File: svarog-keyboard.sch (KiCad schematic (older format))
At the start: 314 parts, among them J1 AVR-ISP-6, J10 I2C, J2 Conn_01x08_Male, J3 I2C, J4 I2C, J5 I2C, J6 I2C, J7 I2C, J8 I2C, J9 I2C, K1 KEYSW, K10 KEYSW, K11 KEYSW, K12 KEYSW, K13 KEYSW, K13-1 KEYSW, K14 KEYSW, K14-1 KEYSW, K14-2 KEYSW, K15 KEYSW, K16 KEYSW, K17 KEYSW, K18 KEYSW, K19 KEYSW, K2 KEYSW, K20 KEYSW, K21 KEYSW, K3 KEYSW, K4 KEYSW, K5 KEYSW, K6 KEYSW, K7 KEYSW, K8 KEYSW, K9 KEYSW, SW1 SW_BOOT, SW2 SW_RESET, U1 ATmega32A-PU, U2 MCP23017_SP, U3 MCP23017_SP, U4 MCP23017_SP, Y1 Crystal

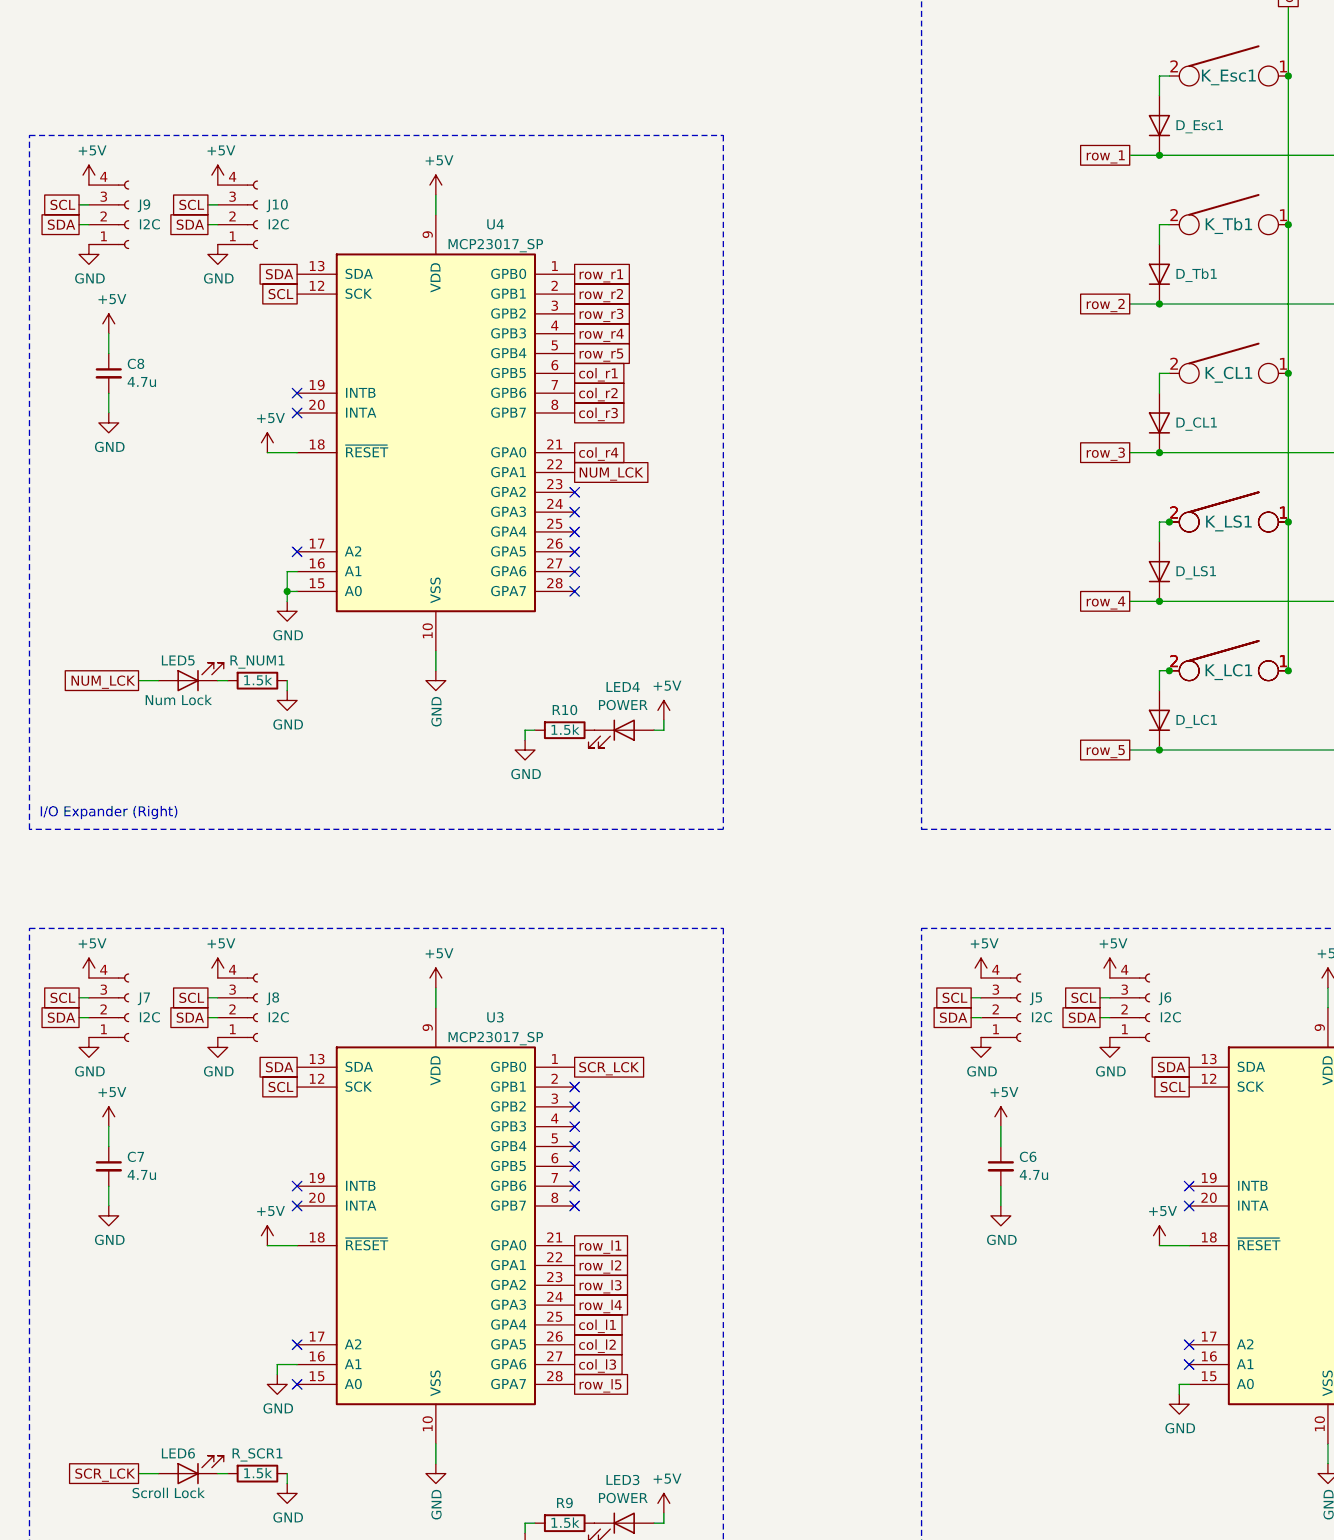
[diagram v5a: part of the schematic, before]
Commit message: Removed Traces, cleanup
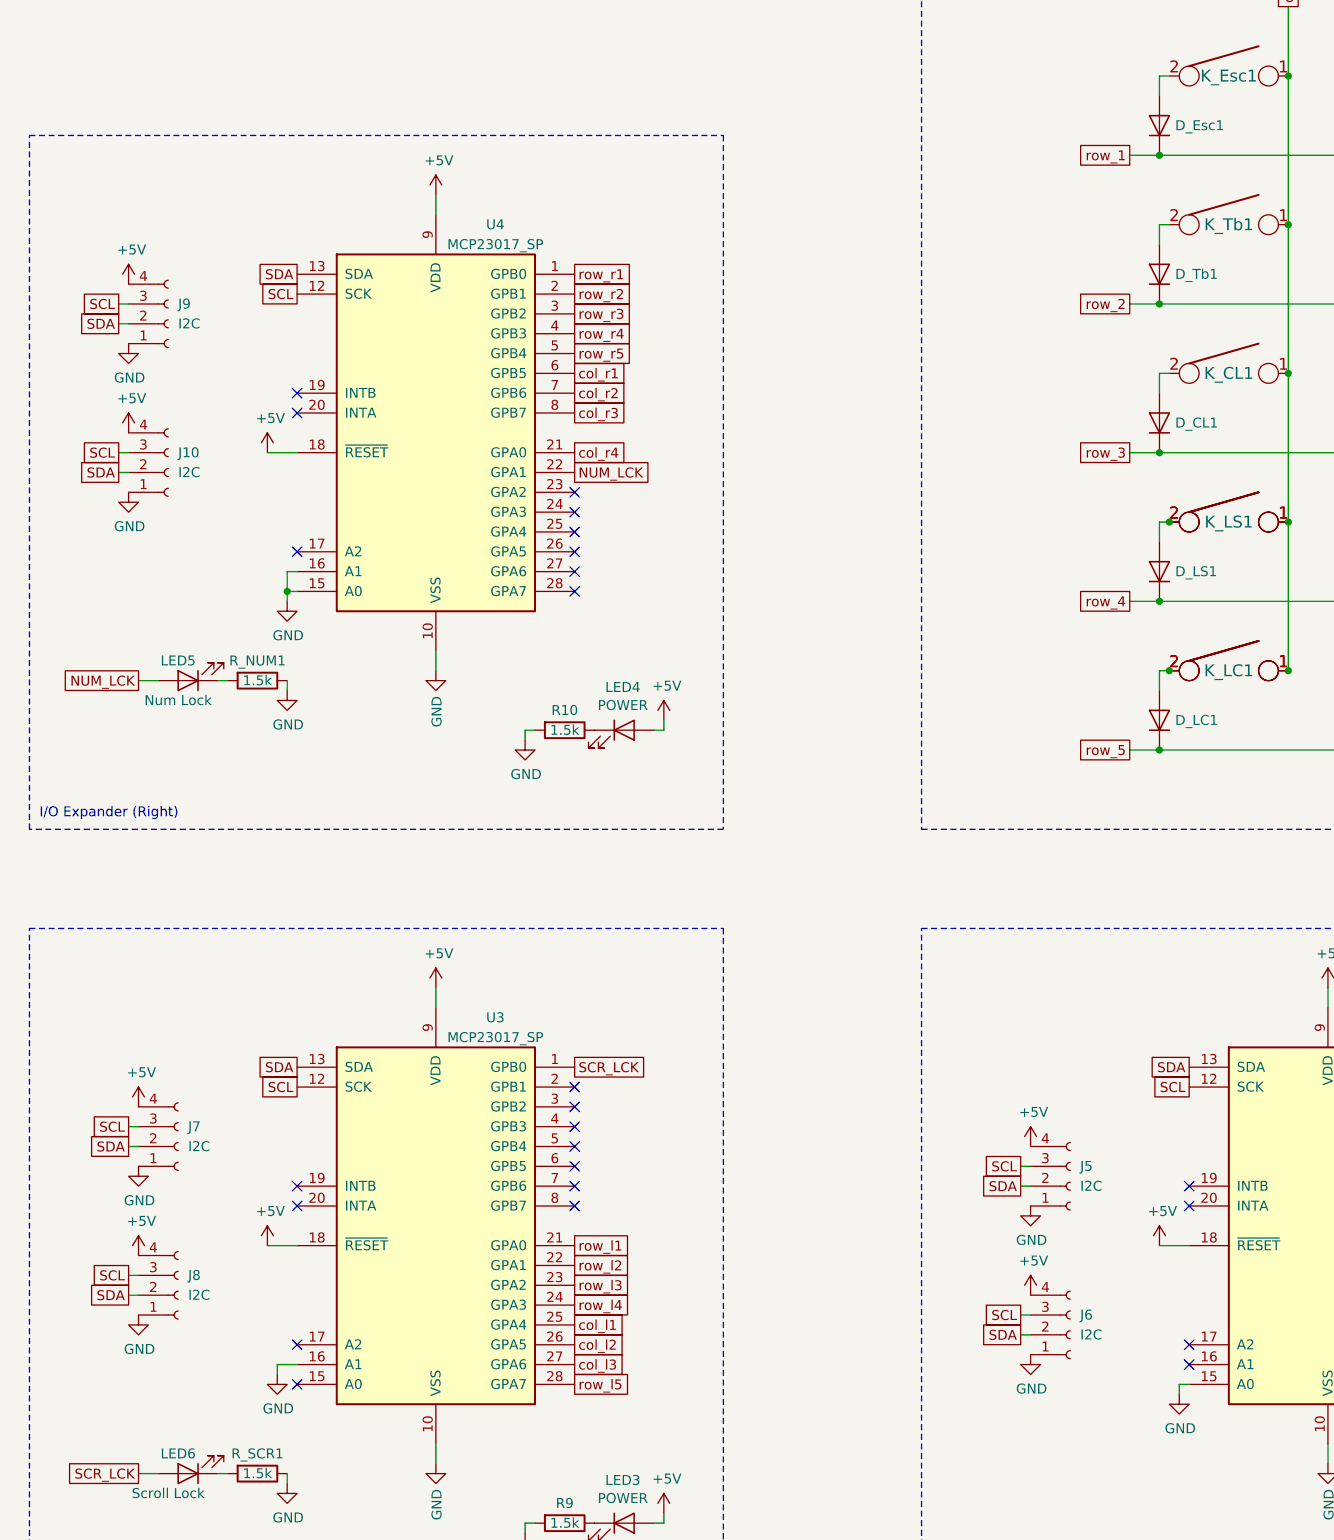
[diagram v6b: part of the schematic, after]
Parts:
- removed C6, C7, C8: 4.7u, Capacitor_THT:CP_Radial_D4.0mm_P1.50mm, symbol Device:C_Small
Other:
- moved on the sheet: J10, J5, J6, J7, J8, J9

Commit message: Wired [TODO] main matrix and [FULL] side matrixes
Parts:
- K_RS1-1.75u1: renamed from K_RS1-1.25u1; footprint Button_Switch_Keyboard:SW_Cherry_MX_1.25u_PCB -> Button_Switch_Keyboard:SW_Cherry_MX_1.75u_PCB
- K_RS1-1u1: renamed from K_RS1-1.5u1; footprint Button_Switch_Keyboard:SW_Cherry_MX_1.50u_PCB -> Button_Switch_Keyboard:SW_Cherry_MX_1.00u_PCB
- K_RS2: footprint Button_Switch_Keyboard:SW_Cherry_MX_1.50u_PCB -> Button_Switch_Keyboard:SW_Cherry_MX_1.00u_PCB
- K_RS2-1.75u1: renamed from K_RS2-1.25u1; footprint Button_Switch_Keyboard:SW_Cherry_MX_1.25u_PCB -> Button_Switch_Keyboard:SW_Cherry_MX_1.75u_PCB
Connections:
- net NUM_LCK: now also U4.1 (GPB0); no longer U4.22 (GPA1)
- net col_1: now also U1.1 (PB0); no longer U1.38 (PA2)
- net col_3: now also U1.2 (PB1); no longer U1.37 (PA3)
- net col_5: now also U1.3 (PB2); no longer U1.36 (PA4)
- net col_r1: now also U4.8 (GPB7); no longer U4.6 (GPB5)
- net col_r3: now also U4.6 (GPB5); no longer U4.8 (GPB7)
- net col_r4: now also U4.5 (GPB4); no longer U4.21 (GPA0)
- net row_1: now also U1.36 (PA4); no longer U1.3 (PB2)
- net row_2: now also U1.37 (PA3); no longer U1.39 (PA1)
- net row_3: now also U1.38 (PA2); no longer U1.2 (PB1)
- net row_4: now also D_RS2.1 (K), U1.39 (PA1); no longer U1.40 (PA0)
- net row_5: now also U1.40 (PA0); no longer U1.1 (PB0)
- net row_r1: now also U4.21 (GPA0); no longer U4.1 (GPB0)
- net row_r2: now also U4.25 (GPA4); no longer U4.2 (GPB1)
- net row_r3: now also U4.26 (GPA5); no longer U4.3 (GPB2)
- net row_r4: now also U4.27 (GPA6); no longer U4.4 (GPB3)
- net row_r5: now also U4.28 (GPA7); no longer U4.5 (GPB4)
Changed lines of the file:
@@
 Wire Wire Line
 	7500 2450 7750 2450
+Text GLabel 3350 1550 2    50   UnSpc ~ 0
+row_4
+Text GLabel 3350 1750 2    50   UnSpc ~ 0
+row_2
+Text GLabel 3350 2350 2    50   UnSpc ~ 0
+col_1
+Text GLabel 3350 2450 2    50   UnSpc ~ 0
+col_3
+Text GLabel 3350 2550 2    50   UnSpc ~ 0
+col_5
 Text GLabel 3350 1450 2    50   UnSpc ~ 0
-row_4
-Text GLabel 3350 1550 2    50   UnSpc ~ 0
-row_2
+row_5
 Text GLabel 3350 1650 2    50   UnSpc ~ 0
-col_1
-Text GLabel 3350 1750 2    50   UnSpc ~ 0
-col_3
+row_3
 Text GLabel 3350 1850 2    50   UnSpc ~ 0
-col_5
-Text GLabel 3350 2350 2    50   UnSpc ~ 0
-row_5
-Text GLabel 3350 2450 2    50   UnSpc ~ 0
-row_3
-Text GLabel 3350 2550 2    50   UnSpc ~ 0
 row_1
 Text GLabel 3350 2650 2    50   UnSpc ~ 0
@@
 NoConn ~ 2350 8900
 NoConn ~ 2350 9600
-NoConn ~ 3750 9700
-NoConn ~ 3750 9800
 Wire Notes Line
 	4500 7500 4500 11000
@@
 Text GLabel 3750 13700 2    50   UnSpc ~ 0
 col_l3
-NoConn ~ 3750 9600
 NoConn ~ 3750 9400
 NoConn ~ 3750 9300
-NoConn ~ 3750 9500
-Text GLabel 3750 8200 2    50   UnSpc ~ 0
-row_r1
-Text GLabel 3750 8300 2    50   UnSpc ~ 0
-row_r2
-Text GLabel 3750 8400 2    50   UnSpc ~ 0
-row_r3
-Text GLabel 3750 8500 2    50   UnSpc ~ 0
-row_r4
-Text GLabel 3750 8600 2    50   UnSpc ~ 0
-row_r5
-Text GLabel 3750 8700 2    50   UnSpc ~ 0
+Text GLabel 3750 8900 2    50   UnSpc ~ 0
 col_r1
 Text GLabel 3750 8800 2    50   UnSpc ~ 0
 col_r2
-Text GLabel 3750 8900 2    50   UnSpc ~ 0
+Text GLabel 3750 8700 2    50   UnSpc ~ 0
 col_r3
-Text GLabel 3750 9100 2    50   UnSpc ~ 0
-col_r4
 $Comp
 L power:GND #PWR0134
@@
 Text GLabel 3350 1950 2    50   UnSpc ~ 0
 CPS_LCK
-Text GLabel 3750 9200 2    50   UnSpc ~ 0
+Text GLabel 3750 8200 2    50   UnSpc ~ 0
 NUM_LCK
 Text GLabel 3750 12200 2    50   UnSpc ~ 0
@@
 Connection ~ 19700 9850
 Wire Wire Line
-	19700 9850 21500 9850
+	19700 9850 20700 9850
 Wire Wire Line
 	20350 8700 20350 9450
@@
 F 0 "K_RS2" H 21050 9450 60  0000 C CNN
 F 1 "KEYSW" H 21050 9350 60  0001 C CNN
-F 2 "Button_Switch_Keyboard:SW_Cherry_MX_1.50u_PCB" H 21050 9450 60  0001 C CNN
+F 2 "Button_Switch_Keyboard:SW_Cherry_MX_1.00u_PCB" H 21050 9450 60  0001 C CNN
 F 3 "" H 21050 9450 60  0000 C CNN
 	1    21050 9450
@@
 	20700 9450 20700 9550
 $Comp
-L keyboard_parts:KEYSW K_RS1-1.5u1
+L keyboard_parts:KEYSW K_RS1-1u1
 U 1 1 5ED8F2CF
 P 20050 9450
-F 0 "K_RS1-1.5u1" H 20050 9450 60  0001 C CNN
+F 0 "K_RS1-1u1" H 20050 9450 60  0001 C CNN
 F 1 "KEYSW" H 20050 9350 60  0001 C CNN
-F 2 "Button_Switch_Keyboard:SW_Cherry_MX_1.50u_PCB" H 20050 9450 60  0001 C CNN
+F 2 "Button_Switch_Keyboard:SW_Cherry_MX_1.00u_PCB" H 20050 9450 60  0001 C CNN
 F 3 "" H 20050 9450 60  0000 C CNN
 	1    20050 9450
@@
 Connection ~ 19750 9450
 $Comp
-L keyboard_parts:KEYSW K_RS1-1.25u1
+L keyboard_parts:KEYSW K_RS1-1.75u1
 U 1 1 5ED919A4
 P 20050 9450
-F 0 "K_RS1-1.25u1" H 20050 9450 60  0001 C CNN
+F 0 "K_RS1-1.75u1" H 20050 9450 60  0001 C CNN
 F 1 "KEYSW" H 20050 9350 60  0001 C CNN
-F 2 "Button_Switch_Keyboard:SW_Cherry_MX_1.25u_PCB" H 20050 9450 60  0001 C CNN
+F 2 "Button_Switch_Keyboard:SW_Cherry_MX_1.75u_PCB" H 20050 9450 60  0001 C CNN
 F 3 "" H 20050 9450 60  0000 C CNN
 	1    20050 9450
@@
 $EndComp
 $Comp
-L keyboard_parts:KEYSW K_RS2-1.25u1
+L keyboard_parts:KEYSW K_RS2-1.75u1
 U 1 1 5ED9613B
 P 21050 9450
-F 0 "K_RS2-1.25u1" H 21050 9450 60  0001 C CNN
+F 0 "K_RS2-1.75u1" H 21050 9450 60  0001 C CNN
 F 1 "KEYSW" H 21050 9350 60  0001 C CNN
-F 2 "Button_Switch_Keyboard:SW_Cherry_MX_1.25u_PCB" H 21050 9450 60  0001 C CNN
+F 2 "Button_Switch_Keyboard:SW_Cherry_MX_1.75u_PCB" H 21050 9450 60  0001 C CNN
 F 3 "" H 21050 9450 60  0000 C CNN
 	1    21050 9450
@@
 NoConn ~ 3750 12500
 NoConn ~ 3750 12600
+Connection ~ 20700 9850
+Wire Wire Line
+	20700 9850 21500 9850
+Text GLabel 3750 9500 2    50   UnSpc ~ 0
+row_r2
+Text GLabel 3750 9600 2    50   UnSpc ~ 0
+row_r3
+Text GLabel 3750 9700 2    50   UnSpc ~ 0
+row_r4
+Text GLabel 3750 9800 2    50   UnSpc ~ 0
+row_r5
+Text GLabel 3750 9100 2    50   UnSpc ~ 0
+row_r1
+Text GLabel 3750 8600 2    50   UnSpc ~ 0
+col_r4
+NoConn ~ 3750 8500
+NoConn ~ 3750 8400
+NoConn ~ 3750 8300
+NoConn ~ 3750 9200
 $EndSCHEMATC
